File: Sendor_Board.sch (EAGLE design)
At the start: 52 parts, among them Q1 8.000Mhz, T1 IRLM6402TRPBF, U1 PIC32MX795F512H-80I/PT, U2 SHT25, U3 MPL115A2, U4 MRF24J40MA, U5 TC1262-3.3VDB, U6 VTX-214-003-105, X1 MINI-USB-SHIELD-UX60A-MB-5ST, X3 MKDSN1,5/4-5,08

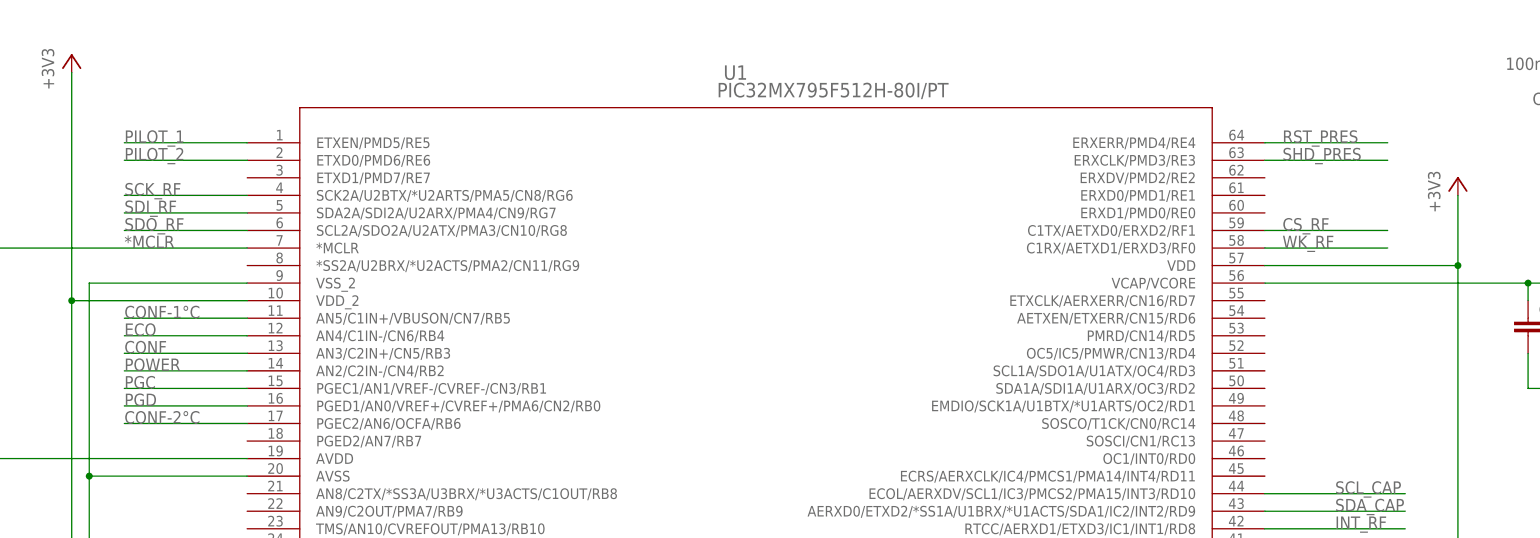
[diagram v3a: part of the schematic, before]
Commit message: Change command PILOT_x from std output to PWM output
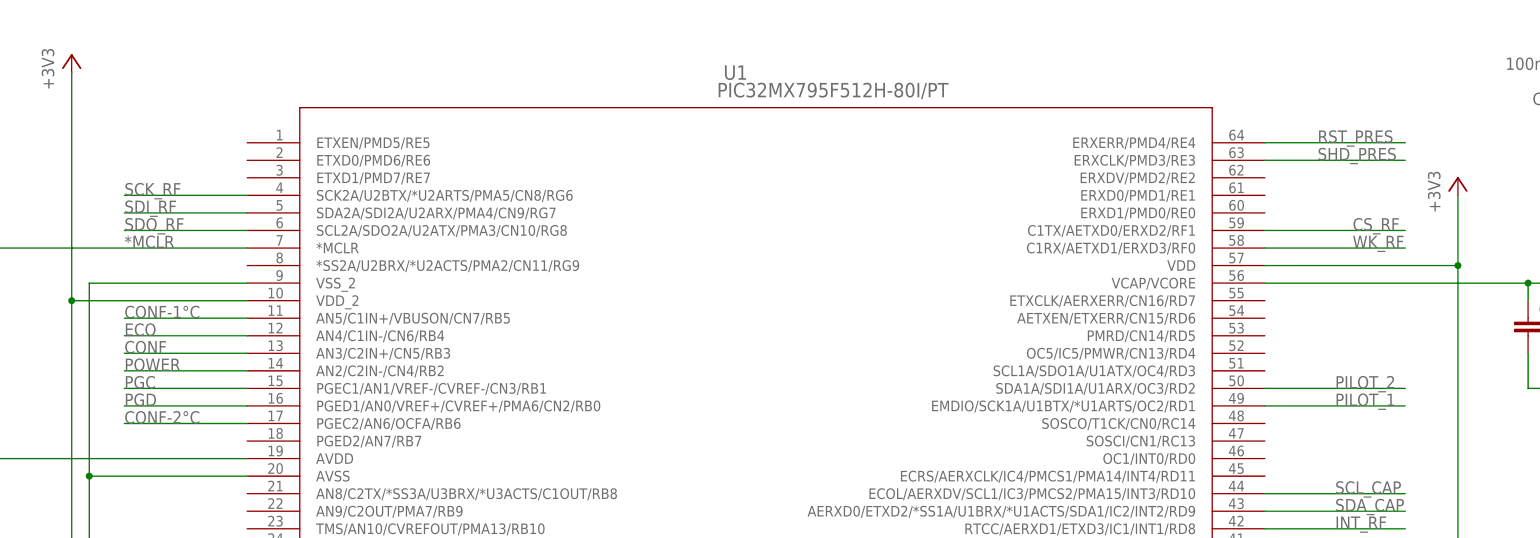
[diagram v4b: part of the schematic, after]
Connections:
- net PILOT_1: now also U1.EMDIO/SCK1A/U1BTX/*U1ARTS/OC2/RD1; no longer U1.ETXEN/PMD5/RE5
- net PILOT_2: now also U1.SDA1A/SDI1A/U1ARX/OC3/RD2; no longer U1.ETXD0/PMD6/RE6
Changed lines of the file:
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@@
 <segment>
 <pinref part="U1" gate="A" pin="ERXERR/PMD4/RE4"/>
-<wire x1="147.32" y1="83.82" x2="165.1" y2="83.82" width="0.1524" layer="91"/>
-<label x="149.86" y="83.82" size="1.778" layer="95"/>
+<wire x1="147.32" y1="83.82" x2="167.64" y2="83.82" width="0.1524" layer="91"/>
+<label x="154.94" y="83.82" size="1.778" layer="95"/>
 </segment>
 </net>
@@
 <segment>
 <pinref part="U1" gate="A" pin="ERXCLK/PMD3/RE3"/>
-<wire x1="147.32" y1="81.28" x2="165.1" y2="81.28" width="0.1524" layer="91"/>
-<label x="149.86" y="81.28" size="1.778" layer="95"/>
+<wire x1="147.32" y1="81.28" x2="167.64" y2="81.28" width="0.1524" layer="91"/>
+<label x="154.94" y="81.28" size="1.778" layer="95"/>
 </segment>
 </net>
@@
 <segment>
 <pinref part="U1" gate="A" pin="C1RX/AETXD1/ERXD3/RF0"/>
-<wire x1="147.32" y1="68.58" x2="165.1" y2="68.58" width="0.1524" layer="91"/>
-<label x="149.86" y="68.58" size="1.778" layer="95"/>
+<wire x1="147.32" y1="68.58" x2="167.64" y2="68.58" width="0.1524" layer="91"/>
+<label x="160.02" y="68.58" size="1.778" layer="95"/>
 </segment>
 </net>
@@
 <segment>
 <pinref part="U1" gate="A" pin="C1TX/AETXD0/ERXD2/RF1"/>
-<wire x1="147.32" y1="71.12" x2="165.1" y2="71.12" width="0.1524" layer="91"/>
-<label x="149.86" y="71.12" size="1.778" layer="95"/>
+<wire x1="147.32" y1="71.12" x2="167.64" y2="71.12" width="0.1524" layer="91"/>
+<label x="160.02" y="71.12" size="1.778" layer="95"/>
 </segment>
 </net>
@@
 <net name="PILOT_1" class="0">
 <segment>
-<pinref part="U1" gate="A" pin="ETXEN/PMD5/RE5"/>
-<wire x1="0" y1="83.82" x2="-17.78" y2="83.82" width="0.1524" layer="91"/>
-<label x="-17.78" y="83.82" size="1.778" layer="95"/>
-</segment>
-<segment>
 <wire x1="53.34" y1="-91.44" x2="66.04" y2="-91.44" width="0.1524" layer="91"/>
 <label x="53.34" y="-91.44" size="1.778" layer="95"/>
 <pinref part="R6" gate="G$1" pin="2"/>
 </segment>
+<segment>
+<pinref part="U1" gate="A" pin="EMDIO/SCK1A/U1BTX/*U1ARTS/OC2/RD1"/>
+<wire x1="147.32" y1="45.72" x2="167.64" y2="45.72" width="0.1524" layer="91"/>
+<label x="157.48" y="45.72" size="1.778" layer="95"/>
+</segment>
 </net>
 <net name="PILOT_2" class="0">
-<segment>
-<pinref part="U1" gate="A" pin="ETXD0/PMD6/RE6"/>
-<wire x1="0" y1="81.28" x2="-17.78" y2="81.28" width="0.1524" layer="91"/>
-<label x="-17.78" y="81.28" size="1.778" layer="95"/>
-</segment>
 <segment>
 <wire x1="53.34" y1="-101.6" x2="66.04" y2="-101.6" width="0.1524" layer="91"/>
@@
 <pinref part="R7" gate="G$1" pin="2"/>
 </segment>
+<segment>
+<pinref part="U1" gate="A" pin="SDA1A/SDI1A/U1ARX/OC3/RD2"/>
+<wire x1="147.32" y1="48.26" x2="167.64" y2="48.26" width="0.1524" layer="91"/>
+<label x="157.48" y="48.26" size="1.778" layer="95"/>
+</segment>
 </net>

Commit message: Move button to int input
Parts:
- added R13: 1k, resistor:R-EU_R1206
- added S1: (no value), switch-omron:31-XX
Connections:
- new net N$21: R13.2, S1.S
- new net SELECT: S1.P, U1.ECRS/AERXCLK/IC4/PMCS1/PMA14/INT4/RD11
- net +3V3: now also R13.1
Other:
- note added: "Select"
- moved on the sheet: CONF, CONF-1°C, CONF-2°C, ECO, POWER, R10, R11, R12, R8, R9
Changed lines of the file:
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@@
 <part name="R11" library="resistor" deviceset="R-EU_" device="R1206" value="1K"/>
 <part name="R12" library="resistor" deviceset="R-EU_" device="R1206" value="1K"/>
+<part name="S1" library="switch-omron" deviceset="31-XX" device=""/>
+<part name="R13" library="resistor" deviceset="R-EU_" device="R1206" value="1k"/>
+<part name="+3V9" library="supply1" deviceset="+3V3" device=""/>
 </parts>
 <sheets>
@@
 <text x="81.28" y="-73.66" size="5.08" layer="97">Electric heater pilot</text>
 <text x="195.58" y="-17.78" size="5.08" layer="97">Power</text>
-<text x="7.62" y="-78.74" size="5.08" layer="97">Led</text>
+<text x="-7.62" y="-78.74" size="5.08" layer="97">Led</text>
+<text x="43.18" y="-119.38" size="5.08" layer="97">Select</text>
 </plain>
 <instances>
@@
 <instance part="GND18" gate="1" x="-35.56" y="-25.4"/>
 <instance part="+3V7" gate="G$1" x="-35.56" y="5.08"/>
-<instance part="+3V8" gate="G$1" x="33.02" y="-81.28"/>
-<instance part="CONF" gate="G$1" x="7.62" y="-101.6" rot="R270"/>
-<instance part="CONF-1°C" gate="G$1" x="7.62" y="-121.92" rot="R270"/>
-<instance part="POWER" gate="G$1" x="7.62" y="-91.44" rot="R270"/>
-<instance part="ECO" gate="G$1" x="7.62" y="-111.76" rot="R270"/>
-<instance part="CONF-2°C" gate="G$1" x="7.62" y="-132.08" rot="R270"/>
-<instance part="R8" gate="G$1" x="20.32" y="-111.76" rot="R180"/>
-<instance part="R9" gate="G$1" x="20.32" y="-101.6" rot="R180"/>
-<instance part="R10" gate="G$1" x="20.32" y="-132.08" rot="R180"/>
-<instance part="R11" gate="G$1" x="20.32" y="-121.92" rot="R180"/>
-<instance part="R12" gate="G$1" x="20.32" y="-91.44" rot="R180"/>
+<instance part="+3V8" gate="G$1" x="17.78" y="-81.28"/>
+<instance part="CONF" gate="G$1" x="-7.62" y="-101.6" rot="R270"/>
+<instance part="CONF-1°C" gate="G$1" x="-7.62" y="-121.92" rot="R270"/>
+<instance part="POWER" gate="G$1" x="-7.62" y="-91.44" rot="R270"/>
+<instance part="ECO" gate="G$1" x="-7.62" y="-111.76" rot="R270"/>
+<instance part="CONF-2°C" gate="G$1" x="-7.62" y="-132.08" rot="R270"/>
+<instance part="R8" gate="G$1" x="5.08" y="-111.76" rot="R180"/>
+<instance part="R9" gate="G$1" x="5.08" y="-101.6" rot="R180"/>
+<instance part="R10" gate="G$1" x="5.08" y="-132.08" rot="R180"/>
+<instance part="R11" gate="G$1" x="5.08" y="-121.92" rot="R180"/>
+<instance part="R12" gate="G$1" x="5.08" y="-91.44" rot="R180"/>
+<instance part="S1" gate="1" x="45.72" y="-132.08" rot="R270"/>
+<instance part="R13" gate="G$1" x="60.96" y="-132.08" rot="R180"/>
+<instance part="+3V9" gate="G$1" x="71.12" y="-124.46"/>
 </instances>
 <busses>
@@
 <pinref part="+3V8" gate="G$1" pin="+3V3"/>
 <pinref part="R12" gate="G$1" pin="1"/>
-<wire x1="33.02" y1="-83.82" x2="33.02" y2="-91.44" width="0.1524" layer="91"/>
-<wire x1="33.02" y1="-91.44" x2="25.4" y2="-91.44" width="0.1524" layer="91"/>
+<wire x1="17.78" y1="-83.82" x2="17.78" y2="-91.44" width="0.1524" layer="91"/>
+<wire x1="17.78" y1="-91.44" x2="10.16" y2="-91.44" width="0.1524" layer="91"/>
 <pinref part="R9" gate="G$1" pin="1"/>
-<wire x1="33.02" y1="-91.44" x2="33.02" y2="-101.6" width="0.1524" layer="91"/>
-<wire x1="33.02" y1="-101.6" x2="25.4" y2="-101.6" width="0.1524" layer="91"/>
-<junction x="33.02" y="-91.44"/>
+<wire x1="17.78" y1="-91.44" x2="17.78" y2="-101.6" width="0.1524" layer="91"/>
+<wire x1="17.78" y1="-101.6" x2="10.16" y2="-101.6" width="0.1524" layer="91"/>
+<junction x="17.78" y="-91.44"/>
 <pinref part="R8" gate="G$1" pin="1"/>
-<wire x1="33.02" y1="-101.6" x2="33.02" y2="-111.76" width="0.1524" layer="91"/>
-<wire x1="33.02" y1="-111.76" x2="25.4" y2="-111.76" width="0.1524" layer="91"/>
-<junction x="33.02" y="-101.6"/>
+<wire x1="17.78" y1="-101.6" x2="17.78" y2="-111.76" width="0.1524" layer="91"/>
+<wire x1="17.78" y1="-111.76" x2="10.16" y2="-111.76" width="0.1524" layer="91"/>
+<junction x="17.78" y="-101.6"/>
 <pinref part="R11" gate="G$1" pin="1"/>
-<wire x1="33.02" y1="-111.76" x2="33.02" y2="-121.92" width="0.1524" layer="91"/>
-<wire x1="33.02" y1="-121.92" x2="25.4" y2="-121.92" width="0.1524" layer="91"/>
-<junction x="33.02" y="-111.76"/>
+<wire x1="17.78" y1="-111.76" x2="17.78" y2="-121.92" width="0.1524" layer="91"/>
+<wire x1="17.78" y1="-121.92" x2="10.16" y2="-121.92" width="0.1524" layer="91"/>
+<junction x="17.78" y="-111.76"/>
 <pinref part="R10" gate="G$1" pin="1"/>
-<wire x1="33.02" y1="-121.92" x2="33.02" y2="-132.08" width="0.1524" layer="91"/>
-<wire x1="33.02" y1="-132.08" x2="25.4" y2="-132.08" width="0.1524" layer="91"/>
-<junction x="33.02" y="-121.92"/>
+<wire x1="17.78" y1="-121.92" x2="17.78" y2="-132.08" width="0.1524" layer="91"/>
+<wire x1="17.78" y1="-132.08" x2="10.16" y2="-132.08" width="0.1524" layer="91"/>
+<junction x="17.78" y="-121.92"/>
+</segment>
+<segment>
+<pinref part="+3V9" gate="G$1" pin="+3V3"/>
+<pinref part="R13" gate="G$1" pin="1"/>
+<wire x1="71.12" y1="-127" x2="71.12" y2="-132.08" width="0.1524" layer="91"/>
+<wire x1="71.12" y1="-132.08" x2="66.04" y2="-132.08" width="0.1524" layer="91"/>
 </segment>
 </net>
@@
 <pinref part="R10" gate="G$1" pin="2"/>
 <pinref part="CONF-2°C" gate="G$1" pin="A"/>
-<wire x1="15.24" y1="-132.08" x2="10.16" y2="-132.08" width="0.1524" layer="91"/>
+<wire x1="0" y1="-132.08" x2="-5.08" y2="-132.08" width="0.1524" layer="91"/>
 </segment>
 </net>
@@
 <pinref part="R11" gate="G$1" pin="2"/>
 <pinref part="CONF-1°C" gate="G$1" pin="A"/>
-<wire x1="15.24" y1="-121.92" x2="10.16" y2="-121.92" width="0.1524" layer="91"/>
+<wire x1="0" y1="-121.92" x2="-5.08" y2="-121.92" width="0.1524" layer="91"/>
 </segment>
 </net>
@@
 <pinref part="R8" gate="G$1" pin="2"/>
 <pinref part="ECO" gate="G$1" pin="A"/>
-<wire x1="15.24" y1="-111.76" x2="10.16" y2="-111.76" width="0.1524" layer="91"/>
+<wire x1="0" y1="-111.76" x2="-5.08" y2="-111.76" width="0.1524" layer="91"/>
 </segment>
 </net>
@@
 <pinref part="R9" gate="G$1" pin="2"/>
 <pinref part="CONF" gate="G$1" pin="A"/>
-<wire x1="15.24" y1="-101.6" x2="10.16" y2="-101.6" width="0.1524" layer="91"/>
+<wire x1="0" y1="-101.6" x2="-5.08" y2="-101.6" width="0.1524" layer="91"/>
 </segment>
 </net>
@@
 <pinref part="R12" gate="G$1" pin="2"/>
 <pinref part="POWER" gate="G$1" pin="A"/>
-<wire x1="15.24" y1="-91.44" x2="10.16" y2="-91.44" width="0.1524" layer="91"/>
+<wire x1="0" y1="-91.44" x2="-5.08" y2="-91.44" width="0.1524" layer="91"/>
 </segment>
 </net>
@@
 <segment>
 <pinref part="POWER" gate="G$1" pin="C"/>
-<wire x1="2.54" y1="-91.44" x2="-10.16" y2="-91.44" width="0.1524" layer="91"/>
-<label x="-10.16" y="-91.44" size="1.778" layer="95"/>
+<wire x1="-12.7" y1="-91.44" x2="-25.4" y2="-91.44" width="0.1524" layer="91"/>
+<label x="-25.4" y="-91.44" size="1.778" layer="95"/>
 </segment>
 <segment>
@@
 <segment>
 <pinref part="CONF" gate="G$1" pin="C"/>
-<wire x1="2.54" y1="-101.6" x2="-10.16" y2="-101.6" width="0.1524" layer="91"/>
-<label x="-10.16" y="-101.6" size="1.778" layer="95"/>
+<wire x1="-12.7" y1="-101.6" x2="-25.4" y2="-101.6" width="0.1524" layer="91"/>
+<label x="-25.4" y="-101.6" size="1.778" layer="95"/>
 </segment>
 <segment>
@@
 <segment>
 <pinref part="ECO" gate="G$1" pin="C"/>
-<wire x1="2.54" y1="-111.76" x2="-10.16" y2="-111.76" width="0.1524" layer="91"/>
-<label x="-10.16" y="-111.76" size="1.778" layer="95"/>
+<wire x1="-12.7" y1="-111.76" x2="-25.4" y2="-111.76" width="0.1524" layer="91"/>
+<label x="-25.4" y="-111.76" size="1.778" layer="95"/>
 </segment>
 <segment>
@@
 <segment>
 <pinref part="CONF-1°C" gate="G$1" pin="C"/>
-<wire x1="2.54" y1="-121.92" x2="-10.16" y2="-121.92" width="0.1524" layer="91"/>
-<label x="-10.16" y="-121.92" size="1.778" layer="95"/>
+<wire x1="-12.7" y1="-121.92" x2="-25.4" y2="-121.92" width="0.1524" layer="91"/>
+<label x="-25.4" y="-121.92" size="1.778" layer="95"/>
 </segment>
 <segment>
@@
 <segment>
 <pinref part="CONF-2°C" gate="G$1" pin="C"/>
-<wire x1="2.54" y1="-132.08" x2="-10.16" y2="-132.08" width="0.1524" layer="91"/>
-<label x="-10.16" y="-132.08" size="1.778" layer="95"/>
+<wire x1="-12.7" y1="-132.08" x2="-25.4" y2="-132.08" width="0.1524" layer="91"/>
+<label x="-25.4" y="-132.08" size="1.778" layer="95"/>
 </segment>
 <segment>
@@
 </segment>
 </net>
+<net name="N$21" class="0">
+<segment>
+<pinref part="R13" gate="G$1" pin="2"/>
+<pinref part="S1" gate="1" pin="S"/>
+<wire x1="55.88" y1="-132.08" x2="50.8" y2="-132.08" width="0.1524" layer="91"/>
+</segment>
+</net>
+<net name="SELECT" class="0">
+<segment>
+<pinref part="S1" gate="1" pin="P"/>
+<wire x1="40.64" y1="-132.08" x2="30.48" y2="-132.08" width="0.1524" layer="91"/>
+<label x="30.48" y="-132.08" size="1.778" layer="95"/>
+</segment>
+<segment>
+<pinref part="U1" gate="A" pin="ECRS/AERXCLK/IC4/PMCS1/PMA14/INT4/RD11"/>
+<wire x1="147.32" y1="35.56" x2="167.64" y2="35.56" width="0.1524" layer="91"/>
+<label x="157.48" y="35.56" size="1.778" layer="95"/>
+</segment>
+</net>
